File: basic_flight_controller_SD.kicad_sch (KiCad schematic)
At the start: 1 part, among them J1 Adafruit 4682 MicroSD SPI bre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

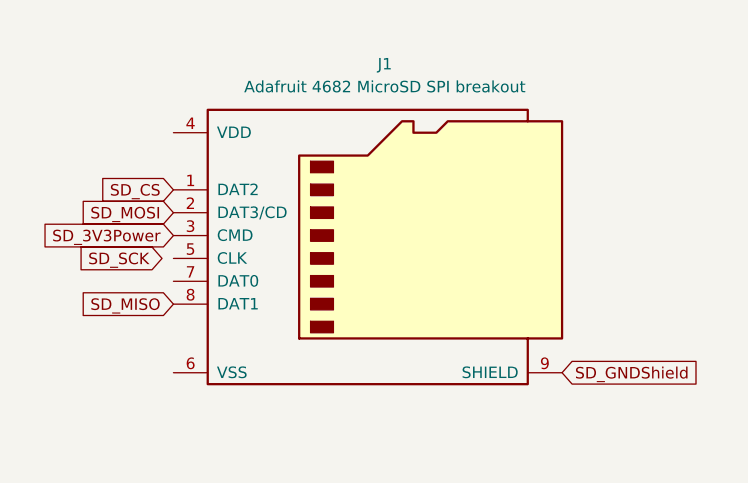
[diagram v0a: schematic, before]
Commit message: Finished the schematic for the SD.
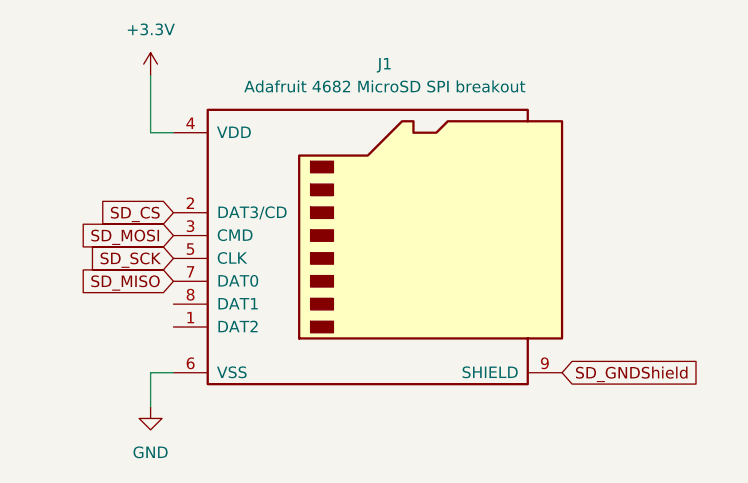
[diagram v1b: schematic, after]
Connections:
- net SD_3V3Power is gone; now on net SD_MOSI: J1.3 (CMD)
- net SD_CS: now also J1.2 (DAT3/CD); no longer J1.1 (DAT2)
- net SD_MISO: now also J1.7 (DAT0); no longer J1.8 (DAT1)
- net SD_MOSI: no longer J1.2 (DAT3/CD)
- net SD_SCK: now also J1.5 (CLK)
- net +3.3V: now reaches J1.4 (VDD)
- net GND: now reaches J1.6 (VSS)
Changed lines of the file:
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@@
 	(generator_version "9.0")
 	(paper "A4")
+	(wire
+		(pts
+			(xy 116.84 92.71) (xy 116.84 96.52)
+		)
+		(stroke
+			(width 0)
+			(type default)
+		)
+	)
+	(wire
+		(pts
+			(xy 116.84 59.69) (xy 116.84 66.04)
+		)
+		(stroke
+			(width 0)
+			(type default)
+		)
+	)
+	(wire
+		(pts
+			(xy 119.38 66.04) (xy 116.84 66.04)
+		)
+		(stroke
+			(width 0)
+			(type default)
+		)
+	)
+	(wire
+		(pts
+			(xy 119.38 92.71) (xy 116.84 92.71)
+		)
+		(stroke
+			(width 0)
+			(type default)
+		)
+	)
+	(global_label "SD_MISO"
+		(shape input)
+		(at 119.38 82.55 180)
+		(fields_autoplaced yes)
+		(effects
+			(font
+				(size 1.27 1.27)
+			)
+			(justify right)
+		)
+		(property "Intersheetrefs" "${INTERSHEET_REFS}"
+			(at 108.3515 82.55 0)
+			(effects
+				(font
+					(size 1.27 1.27)
+				)
+				(justify right)
+				(hide yes)
+			)
+		)
+	)
 	(global_label "SD_CS"
 		(shape input)
-		(at 119.38 72.39 180)
-		(fields_autoplaced yes)
-		(effects
-			(font
-				(size 1.27 1.27)
-			)
-			(justify right)
-		)
-		(property "Intersheetrefs" "${INTERSHEET_REFS}"
-			(at 110.4682 72.39 0)
+		(at 119.38 74.93 180)
+		(fields_autoplaced yes)
+		(effects
+			(font
+				(size 1.27 1.27)
+			)
+			(justify right)
+		)
+		(property "Intersheetrefs" "${INTERSHEET_REFS}"
+			(at 110.4682 74.93 0)
 			(effects
 				(font
@@
 	(global_label "SD_MOSI"
 		(shape input)
-		(at 119.38 74.93 180)
-		(fields_autoplaced yes)
-		(effects
-			(font
-				(size 1.27 1.27)
-			)
-			(justify right)
-		)
-		(property "Intersheetrefs" "${INTERSHEET_REFS}"
-			(at 108.3515 74.93 0)
+		(at 119.38 77.47 180)
+		(fields_autoplaced yes)
+		(effects
+			(font
+				(size 1.27 1.27)
+			)
+			(justify right)
+		)
+		(property "Intersheetrefs" "${INTERSHEET_REFS}"
+			(at 108.3515 77.47 0)
 			(effects
 				(font
@@
 	(global_label "SD_SCK"
 		(shape input)
-		(at 118.11 80.01 180)
-		(fields_autoplaced yes)
-		(effects
-			(font
-				(size 1.27 1.27)
-			)
-			(justify right)
-		)
-		(property "Intersheetrefs" "${INTERSHEET_REFS}"
-			(at 107.9282 80.01 0)
-			(effects
-				(font
-					(size 1.27 1.27)
-				)
-				(justify right)
-				(hide yes)
-			)
-		)
-	)
-	(global_label "SD_MISO"
-		(shape input)
-		(at 119.38 85.09 180)
-		(fields_autoplaced yes)
-		(effects
-			(font
-				(size 1.27 1.27)
-			)
-			(justify right)
-		)
-		(property "Intersheetrefs" "${INTERSHEET_REFS}"
-			(at 108.3515 85.09 0)
-			(effects
-				(font
-					(size 1.27 1.27)
-				)
-				(justify right)
-				(hide yes)
-			)
-		)
-	)
-	(global_label "SD_3V3Power"
-		(shape input)
-		(at 119.38 77.47 180)
-		(fields_autoplaced yes)
-		(effects
-			(font
-				(size 1.27 1.27)
-			)
-			(justify right)
-		)
-		(property "Intersheetrefs" "${INTERSHEET_REFS}"
-			(at 103.8158 77.47 0)
+		(at 119.38 80.01 180)
+		(fields_autoplaced yes)
+		(effects
+			(font
+				(size 1.27 1.27)
+			)
+			(justify right)
+		)
+		(property "Intersheetrefs" "${INTERSHEET_REFS}"
+			(at 109.1982 80.01 0)
 			(effects
 				(font
@@
 			)
 		)
+	)
+	(symbol
+		(lib_id "power:GND")
+		(at 116.84 96.52 0)
+		(unit 1)
+		(exclude_from_sim no)
+		(in_bom yes)
+		(on_board yes)
+		(dnp no)
+		(fields_autoplaced yes)
+		(property "Reference" "#PWR09"
+			(at 116.84 102.87 0)
+			(effects
+				(font
+					(size 1.27 1.27)
+				)
+				(hide yes)
+			)
+		)
+		(property "Value" "GND"
+			(at 116.84 101.6 0)
+			(effects
+				(font
+					(size 1.27 1.27)
+				)
+			)
+		)
+		(property "Footprint" ""
+			(at 116.84 96.52 0)
+			(effects
+				(font
+					(size 1.27 1.27)
+				)
+				(hide yes)
+			)
+		)
+		(property "Datasheet" ""
+			(at 116.84 96.52 0)
+			(effects
+				(font
+					(size 1.27 1.27)
+				)
+				(hide yes)
+			)
+		)
+		(property "Description" "Power symbol creates a global label with name \"GND\" , ground"
+			(at 116.84 96.52 0)
+			(effects
+				(font
+					(size 1.27 1.27)
+				)
+				(hide yes)
+			)
+		)
+		(pin "1"
+		)
+		(instances
+			(project ""
+				(path "/e04fbe87-dc7c-407c-abef-b71ed1bbe06a/1772bb2a-be08-410e-8d4b-a91b7731fae6"
+					(reference "#PWR09")
+					(unit 1)
+				)
+			)
+		)
+	)
+	(symbol
+		(lib_id "power:+3.3V")
+		(at 116.84 59.69 0)
+		(unit 1)
+		(exclude_from_sim no)
+		(in_bom yes)
+		(on_board yes)
+		(dnp no)
+		(fields_autoplaced yes)
+		(property "Reference" "#PWR010"
+			(at 116.84 63.5 0)
+			(effects
+				(font
+					(size 1.27 1.27)
+				)
+				(hide yes)
+			)
+		)
+		(property "Value" "+3.3V"
+			(at 116.84 54.61 0)
+			(effects
+				(font
+					(size 1.27 1.27)
+				)
+			)
+		)
+		(property "Footprint" ""
+			(at 116.84 59.69 0)
+			(effects
+				(font
+					(size 1.27 1.27)
+				)
+				(hide yes)
+			)
+		)
+		(property "Datasheet" ""
+			(at 116.84 59.69 0)
+			(effects
+				(font
+					(size 1.27 1.27)
+				)
+				(hide yes)
+			)
+		)
+		(property "Description" "Power symbol creates a global label with name \"+3.3V\""
+			(at 116.84 59.69 0)
+			(effects
+				(font
+					(size 1.27 1.27)
+				)
+				(hide yes)
+			)
+		)
+		(pin "1"
+		)
+		(instances
+			(project ""
+				(path "/e04fbe87-dc7c-407c-abef-b71ed1bbe06a/1772bb2a-be08-410e-8d4b-a91b7731fae6"
+					(reference "#PWR010")
+					(unit 1)
+				)
+			)
+		)
